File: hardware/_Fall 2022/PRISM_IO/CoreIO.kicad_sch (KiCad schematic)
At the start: 26 parts, among them J1 CORE_FC, J2 COTS_SWITCH_PLUG, J3 PYRO 1, J4 PYRO 2, Q1 Q_NJFET_DGS, Q2 Q_NJFET_DGS

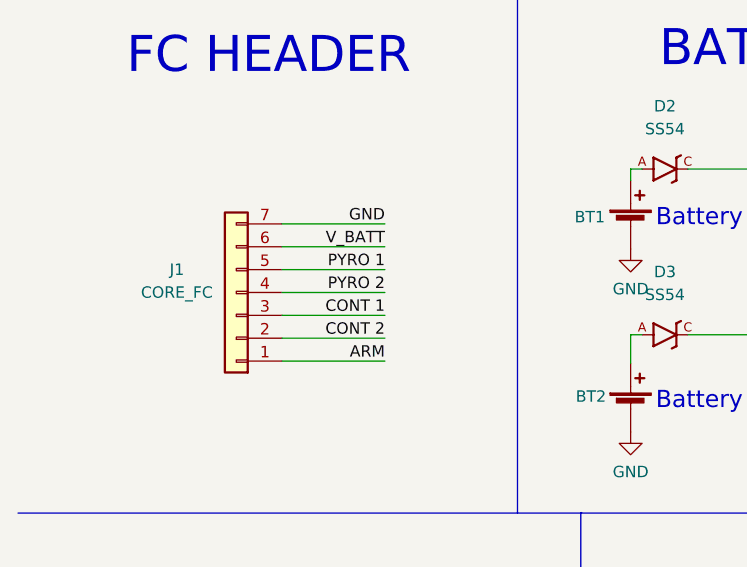
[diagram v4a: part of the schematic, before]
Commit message: Switch connector pin order on IO
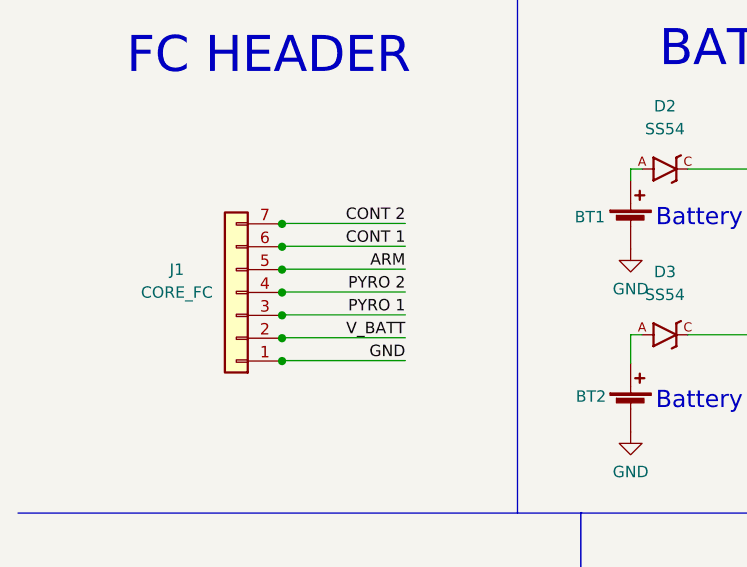
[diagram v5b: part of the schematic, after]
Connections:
- net ARM: now also J1.5 (Pin_5); no longer J1.1 (Pin_1)
- net CONT 1: now also J1.6 (Pin_6); no longer J1.3 (Pin_3)
- net CONT 2: now also J1.7 (Pin_7); no longer J1.2 (Pin_2)
- net GND: now also J1.1 (Pin_1); no longer J1.7 (Pin_7)
- net PYRO 1: now also J1.3 (Pin_3); no longer J1.5 (Pin_5)
- net V_BATT: now also J1.2 (Pin_2); no longer J1.6 (Pin_6)
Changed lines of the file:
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@@
   (junction (at 159.385 40.005) (diameter 0) (color 0 0 0 0)
   )
+  (junction (at 41.275 52.451) (diameter 0) (color 0 0 0 0)
+  )
   (junction (at 41.529 118.618) (diameter 0) (color 0 0 0 0)
   )
@@
   (junction (at 202.565 48.895) (diameter 0) (color 0 0 0 0)
   )
+  (junction (at 41.275 47.371) (diameter 0) (color 0 0 0 0)
+  )
   (junction (at 58.039 131.318) (diameter 0) (color 0 0 0 0)
   )
   (junction (at 87.884 133.223) (diameter 0) (color 0 0 0 0)
   )
+  (junction (at 41.275 37.211) (diameter 0) (color 0 0 0 0)
+  )
   (junction (at 117.094 130.683) (diameter 0) (color 0 0 0 0)
   )
+  (junction (at 41.275 39.751) (diameter 0) (color 0 0 0 0)
+  )
+  (junction (at 41.275 42.291) (diameter 0) (color 0 0 0 0)
+  )
   (junction (at 102.235 31.115) (diameter 0) (color 0 0 0 0)
   )
+  (junction (at 41.275 44.831) (diameter 0) (color 0 0 0 0)
+  )
   (junction (at 211.455 37.465) (diameter 0) (color 0 0 0 0)
   )
+  (junction (at 41.275 49.911) (diameter 0) (color 0 0 0 0)
+  )
   (wire (pts (xy 117.094 142.113) (xy 117.094 145.923))
     (stroke (width 0) (type default) (color 0 0 0 0))
@@
     (stroke (width 0) (type default) (color 0 0 0 0))
   )
-  (wire (pts (xy 52.705 44.831) (xy 41.275 44.831))
-    (stroke (width 0) (type default) (color 0 0 0 0))
-  )
   (wire (pts (xy 245.745 50.165) (xy 245.745 43.18))
     (stroke (width 0) (type default) (color 0 0 0 0))
@@
     (stroke (width 0) (type default) (color 0 0 0 0))
   )
-  (wire (pts (xy 52.705 47.371) (xy 41.275 47.371))
-    (stroke (width 0) (type default) (color 0 0 0 0))
-  )
   (wire (pts (xy 159.385 47.625) (xy 159.385 50.165))
     (stroke (width 0) (type default) (color 0 0 0 0))
@@
     (stroke (width 0) (type default) (color 0 0 0 0))
   )
+  (wire (pts (xy 41.275 44.7789) (xy 41.275 44.831))
+    (stroke (width 0) (type default) (color 0 0 0 0))
+  )
+  (wire (pts (xy 41.275 47.3189) (xy 41.275 47.371))
+    (stroke (width 0) (type default) (color 0 0 0 0))
+  )
+  (wire (pts (xy 41.275 44.7789) (xy 54.9741 44.7789))
+    (stroke (width 0) (type default) (color 0 0 0 0))
+  )
   (wire (pts (xy 207.645 32.385) (xy 207.645 34.29))
     (stroke (width 0) (type default) (color 0 0 0 0))
@@
     (stroke (width 0) (type default) (color 0 0 0 0))
   )
-  (wire (pts (xy 52.705 39.751) (xy 41.275 39.751))
-    (stroke (width 0) (type default) (color 0 0 0 0))
-  )
   (polyline (pts (xy 117.983 12.192) (xy 117.983 69.342))
     (stroke (width 0) (type default) (color 0 0 0 0))
   )
+  (wire (pts (xy 41.275 37.1589) (xy 41.275 37.211))
+    (stroke (width 0) (type default) (color 0 0 0 0))
+  )
   (wire (pts (xy 58.039 126.238) (xy 58.039 131.318))
     (stroke (width 0) (type default) (color 0 0 0 0))
@@
     (stroke (width 0) (type default) (color 0 0 0 0))
   )
-  (wire (pts (xy 52.705 49.911) (xy 41.275 49.911))
-    (stroke (width 0) (type default) (color 0 0 0 0))
-  )
   (wire (pts (xy 100.584 117.983) (xy 100.584 128.143))
     (stroke (width 0) (type default) (color 0 0 0 0))
   )
+  (wire (pts (xy 41.275 37.1589) (xy 54.9741 37.1589))
+    (stroke (width 0) (type default) (color 0 0 0 0))
+  )
   (wire (pts (xy 58.039 142.748) (xy 58.039 146.558))
     (stroke (width 0) (type default) (color 0 0 0 0))
@@
     (stroke (width 0) (type default) (color 0 0 0 0))
   )
+  (wire (pts (xy 41.275 49.8589) (xy 41.275 49.911))
+    (stroke (width 0) (type default) (color 0 0 0 0))
+  )
   (wire (pts (xy 28.829 145.288) (xy 28.829 149.098))
     (stroke (width 0) (type default) (color 0 0 0 0))
@@
     (stroke (width 0) (type default) (color 0 0 0 0))
   )
+  (wire (pts (xy 41.275 47.3189) (xy 54.9741 47.3189))
+    (stroke (width 0) (type default) (color 0 0 0 0))
+  )
   (wire (pts (xy 277.495 40.005) (xy 277.495 50.165))
     (stroke (width 0) (type default) (color 0 0 0 0))
@@
     (stroke (width 0) (type default) (color 0 0 0 0))
   )
+  (wire (pts (xy 41.275 42.2389) (xy 54.9741 42.2389))
+    (stroke (width 0) (type default) (color 0 0 0 0))
+  )
   (wire (pts (xy 211.455 37.465) (xy 211.455 51.435))
     (stroke (width 0) (type default) (color 0 0 0 0))
   )
+  (wire (pts (xy 41.275 52.3989) (xy 41.275 52.451))
+    (stroke (width 0) (type default) (color 0 0 0 0))
+  )
   (wire (pts (xy 270.51 34.925) (xy 273.685 34.925))
     (stroke (width 0) (type default) (color 0 0 0 0))
@@
     (stroke (width 0) (type default) (color 0 0 0 0))
   )
+  (wire (pts (xy 41.275 49.8589) (xy 54.9741 49.8589))
+    (stroke (width 0) (type default) (color 0 0 0 0))
+  )
   (wire (pts (xy 41.529 138.938) (xy 41.529 149.098))
     (stroke (width 0) (type default) (color 0 0 0 0))
   )
-  (wire (pts (xy 52.705 52.451) (xy 41.275 52.451))
+  (wire (pts (xy 41.275 39.6989) (xy 41.275 39.751))
     (stroke (width 0) (type default) (color 0 0 0 0))
   )
@@
     (stroke (width 0) (type default) (color 0 0 0 0))
   )
+  (wire (pts (xy 41.275 39.6989) (xy 54.9741 39.6989))
+    (stroke (width 0) (type default) (color 0 0 0 0))
+  )
   (wire (pts (xy 145.415 38.735) (xy 149.225 38.735))
     (stroke (width 0) (type default) (color 0 0 0 0))
@@
     (stroke (width 0) (type default) (color 0 0 0 0))
   )
+  (wire (pts (xy 41.275 42.2389) (xy 41.275 42.291))
+    (stroke (width 0) (type default) (color 0 0 0 0))
+  )
   (wire (pts (xy 270.51 45.085) (xy 273.685 45.085))
     (stroke (width 0) (type default) (color 0 0 0 0))
@@
     (stroke (width 0) (type default) (color 0 0 0 0))
   )
-  (wire (pts (xy 52.705 37.211) (xy 41.275 37.211))
-    (stroke (width 0) (type default) (color 0 0 0 0))
-  )
   (polyline (pts (xy 117.983 69.342) (xy 177.8 69.342))
     (stroke (width 0) (type default) (color 0 0 0 0))
@@
     (stroke (width 0) (type default) (color 0 0 0 0))
   )
+  (wire (pts (xy 41.275 52.3989) (xy 54.9741 52.3989))
+    (stroke (width 0) (type default) (color 0 0 0 0))
+  )
   (polyline (pts (xy 136.144 161.29) (xy 136.144 69.2404))
     (stroke (width 0) (type default) (color 0 0 0 0))
@@
   )
   (polyline (pts (xy 136.144 69.2404) (xy 136.271 69.2404))
-    (stroke (width 0) (type default) (color 0 0 0 0))
-  )
-  (wire (pts (xy 52.705 42.291) (xy 41.275 42.291))
     (stroke (width 0) (type default) (color 0 0 0 0))
   )
@@
     (effects (font (size 1.27 1.27)) (justify right bottom))
   )
+  (label "V_BATT" (at 54.9741 49.8589 180)
+    (effects (font (size 1.27 1.27)) (justify right bottom))
+  )
   (label "CONT 1" (at 63.119 131.318 0)
     (effects (font (size 1.27 1.27)) (justify left bottom))
@@
     (effects (font (size 1.27 1.27)) (justify left bottom))
   )
-  (label "CONT 2" (at 52.705 49.911 180)
+  (label "CONT 2" (at 54.9741 37.1589 180)
+    (effects (font (size 1.27 1.27)) (justify right bottom))
+  )
+  (label "ARM" (at 54.9741 42.2389 180)
     (effects (font (size 1.27 1.27)) (justify right bottom))
   )
@@
     (effects (font (size 1.27 1.27)) (justify right bottom))
   )
-  (label "PYRO 2" (at 52.705 44.831 180)
-    (effects (font (size 1.27 1.27)) (justify right bottom))
-  )
   (label "V_BATT" (at 186.055 29.845 180)
     (effects (font (size 1.27 1.27)) (justify right bottom))
   )
+  (label "GND" (at 54.9741 52.3989 180)
+    (effects (font (size 1.27 1.27)) (justify right bottom))
+  )
   (label "V_IGNITOR" (at 211.455 51.435 0)
     (effects (font (size 1.27 1.27)) (justify left bottom))
@@
     (effects (font (size 1.27 1.27)) (justify left bottom))
   )
-  (label "CONT 1" (at 52.705 47.371 180)
-    (effects (font (size 1.27 1.27)) (justify right bottom))
-  )
   (label "SWITCH1" (at 106.68 31.115 0)
     (effects (font (size 1.27 1.27)) (justify left bottom))
   )
+  (label "PYRO 1" (at 54.9741 47.3189 180)
+    (effects (font (size 1.27 1.27)) (justify right bottom))
+  )
   (label "PYRO 2" (at 77.724 133.223 0)
     (effects (font (size 1.27 1.27)) (justify left bottom))
@@
     (effects (font (size 1.27 1.27)) (justify left bottom))
   )
-  (label "GND" (at 52.705 37.211 180)
-    (effects (font (size 1.27 1.27)) (justify right bottom))
-  )
-  (label "V_BATT" (at 52.705 39.751 180)
+  (label "PYRO 2" (at 54.9741 44.7789 180)
     (effects (font (size 1.27 1.27)) (justify right bottom))
   )
@@
     (effects (font (size 1.27 1.27)) (justify left bottom))
   )
-  (label "PYRO 1" (at 52.705 42.291 180)
-    (effects (font (size 1.27 1.27)) (justify right bottom))
-  )
-  (label "ARM" (at 52.705 52.451 180)
-    (effects (font (size 1.27 1.27)) (justify right bottom))
-  )
+  (label "CONT 1" (at 54.9741 39.6989 180)
+    (effects (font (size 1.27 1.27)) (justify right bottom))
+  )

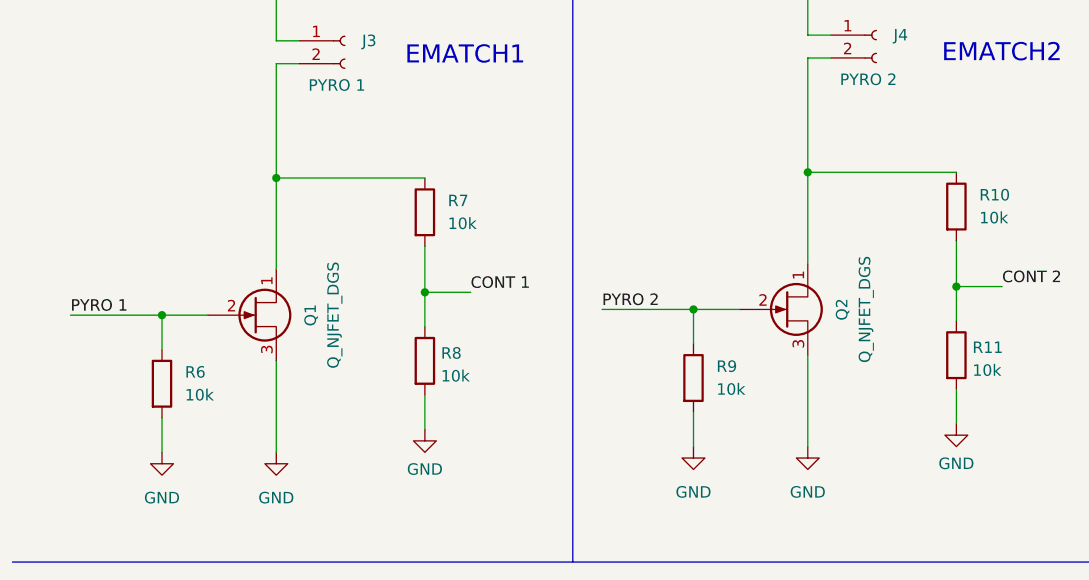
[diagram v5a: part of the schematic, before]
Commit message: Add MOSFET
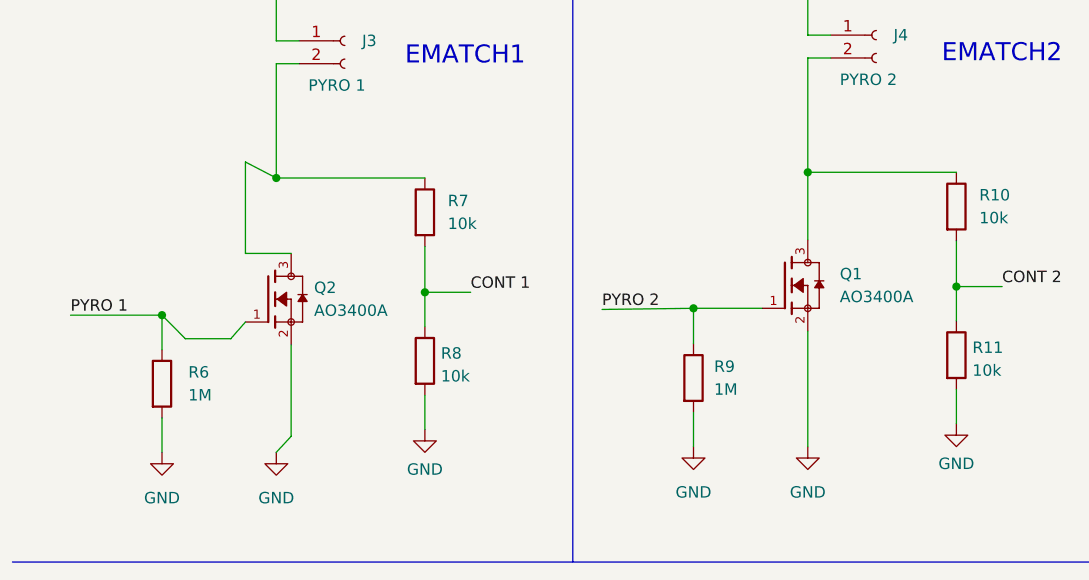
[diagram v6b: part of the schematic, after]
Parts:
- removed Q1, Q2: Q_NJFET_DGS, symbol Device:Q_NJFET_DGS
- added Q1, Q2: AO3400A, SOT95P280X125-3N, symbol AO3400A:AO3400A
- R6, R9: value 10k -> 1M
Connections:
- net GND: now also Q1.2, Q2.2
- net PYRO 1: now also Q2.1
- net PYRO 2: now also Q1.1
- net at J4.2 (Pin_2), R10.1: now also Q1.3
- net at J3.2 (Pin_2), R7.1: now also Q2.3

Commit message: add cad models
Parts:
- Q1: footprint SOT95P280X125-3N -> AO3400A:SOT95P280X125-3N; Vendor (none) -> C20917
- Q2: Vendor (none) -> C20917
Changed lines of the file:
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@@
       (effects (font (size 1.27 1.27)) (justify bottom) hide)
+    )
+    (property "Vendor" "C20917" (id 8) (at 40.64 132.08 0)
+      (effects (font (size 1.27 1.27)) hide)
     )
     (pin "1")
@@
       (effects (font (size 1.27 1.27)) (justify left))
     )
-    (property "Footprint" "SOT95P280X125-3N" (id 2) (at 98.044 130.556 0)
+    (property "Footprint" "AO3400A:SOT95P280X125-3N" (id 2) (at 98.044 130.556 0)
       (effects (font (size 1.27 1.27)) (justify bottom) hide)
     )
@@
     (property "PARTREV" "L" (id 7) (at 98.044 130.556 0)
       (effects (font (size 1.27 1.27)) (justify bottom) hide)
+    )
+    (property "Vendor" "C20917" (id 8) (at 98.044 130.556 0)
+      (effects (font (size 1.27 1.27)) hide)
     )
     (pin "1")
@@
     )
     (path "/b5a71cfa-f75d-4518-aa9f-ad067f3610b5"
-      (reference "Q1") (unit 1) (value "AO3400A") (footprint "SOT95P280X125-3N")
+      (reference "Q1") (unit 1) (value "AO3400A") (footprint "AO3400A:SOT95P280X125-3N")
     )
     (path "/2abb36cb-2815-40ea-891e-b0d077e41256"

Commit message: io layout
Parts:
- D1: Vendor (none) -> C2290
- D2, D3: Vendor (none) -> C22452
- R1: Vendor (none) -> C22808
- R10, R11, R2, R5, R7, R8: Vendor (none) -> C25804
- R6, R9: Vendor (none) -> C22935
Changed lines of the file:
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@@
+      (effects (font (size 1.27 1.27)) hide)
+    )
+    (property "Vendor" "C2290" (id 4) (at 159.385 43.815 90)
       (effects (font (size 1.27 1.27)) hide)
     )
@@
       (effects (font (size 1.27 1.27)) hide)
     )
+    (property "Vendor" "C25804" (id 4) (at 117.094 121.793 0)
+      (effects (font (size 1.27 1.27)) hide)
+    )
     (pin "1")
     (pin "2")
@@
     )
     (property "Datasheet" "~" (id 3) (at 159.385 53.975 0)
+      (effects (font (size 1.27 1.27)) hide)
+    )
+    (property "Vendor" "C22808" (id 4) (at 159.385 53.975 0)
       (effects (font (size 1.27 1.27)) hide)
     )
@@
       (effects (font (size 1.27 1.27)) hide)
     )
+    (property "Vendor" "C22452" (id 4) (at 83.82 31.115 0)
+      (effects (font (size 1.27 1.27)) hide)
+    )
     (pin "A")
     (pin "C")
@@
       (effects (font (size 1.27 1.27)) hide)
     )
+    (property "Vendor" "C22935" (id 4) (at 87.884 140.843 0)
+      (effects (font (size 1.27 1.27)) hide)
+    )
     (pin "1")
     (pin "2")
@@
       (effects (font (size 1.27 1.27)) hide)
     )
+    (property "Vendor" "C25804" (id 4) (at 58.039 122.428 0)
+      (effects (font (size 1.27 1.27)) hide)
+    )
     (pin "1")
     (pin "2")
@@
     )
     (property "Datasheet" "~" (id 3) (at 28.829 141.478 0)
+      (effects (font (size 1.27 1.27)) hide)
+    )
+    (property "Vendor" "C22935" (id 4) (at 28.829 141.478 0)
       (effects (font (size 1.27 1.27)) hide)
     )
@@
       (effects (font (size 1.27 1.27)) hide)
     )
+    (property "Vendor" "C22452" (id 4) (at 83.82 49.53 0)
+      (effects (font (size 1.27 1.27)) hide)
+    )
     (pin "A")
     (pin "C")
@@
       (effects (font (size 1.27 1.27)) hide)
     )
+    (property "Vendor" "C25804" (id 4) (at 202.565 43.815 0)
+      (effects (font (size 1.27 1.27)) hide)
+    )
     (pin "1")
     (pin "2")
@@
     )
     (property "Datasheet" "~" (id 3) (at 117.094 138.303 0)
+      (effects (font (size 1.27 1.27)) hide)
+    )
+    (property "Vendor" "C25804" (id 4) (at 117.094 138.303 0)
       (effects (font (size 1.27 1.27)) hide)
     )
@@
       (effects (font (size 1.27 1.27)) hide)
     )
+    (property "Vendor" "C25804" (id 4) (at 202.565 55.245 0)
+      (effects (font (size 1.27 1.27)) hide)
+    )
     (pin "1")
     (pin "2")
@@
       (effects (font (size 1.27 1.27)) hide)
     )
+    (property "Vendor" "C25804" (id 4) (at 58.039 138.938 0)
+      (effects (font (size 1.27 1.27)) hide)
+    )
